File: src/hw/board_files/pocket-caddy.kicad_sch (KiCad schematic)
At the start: 6 parts

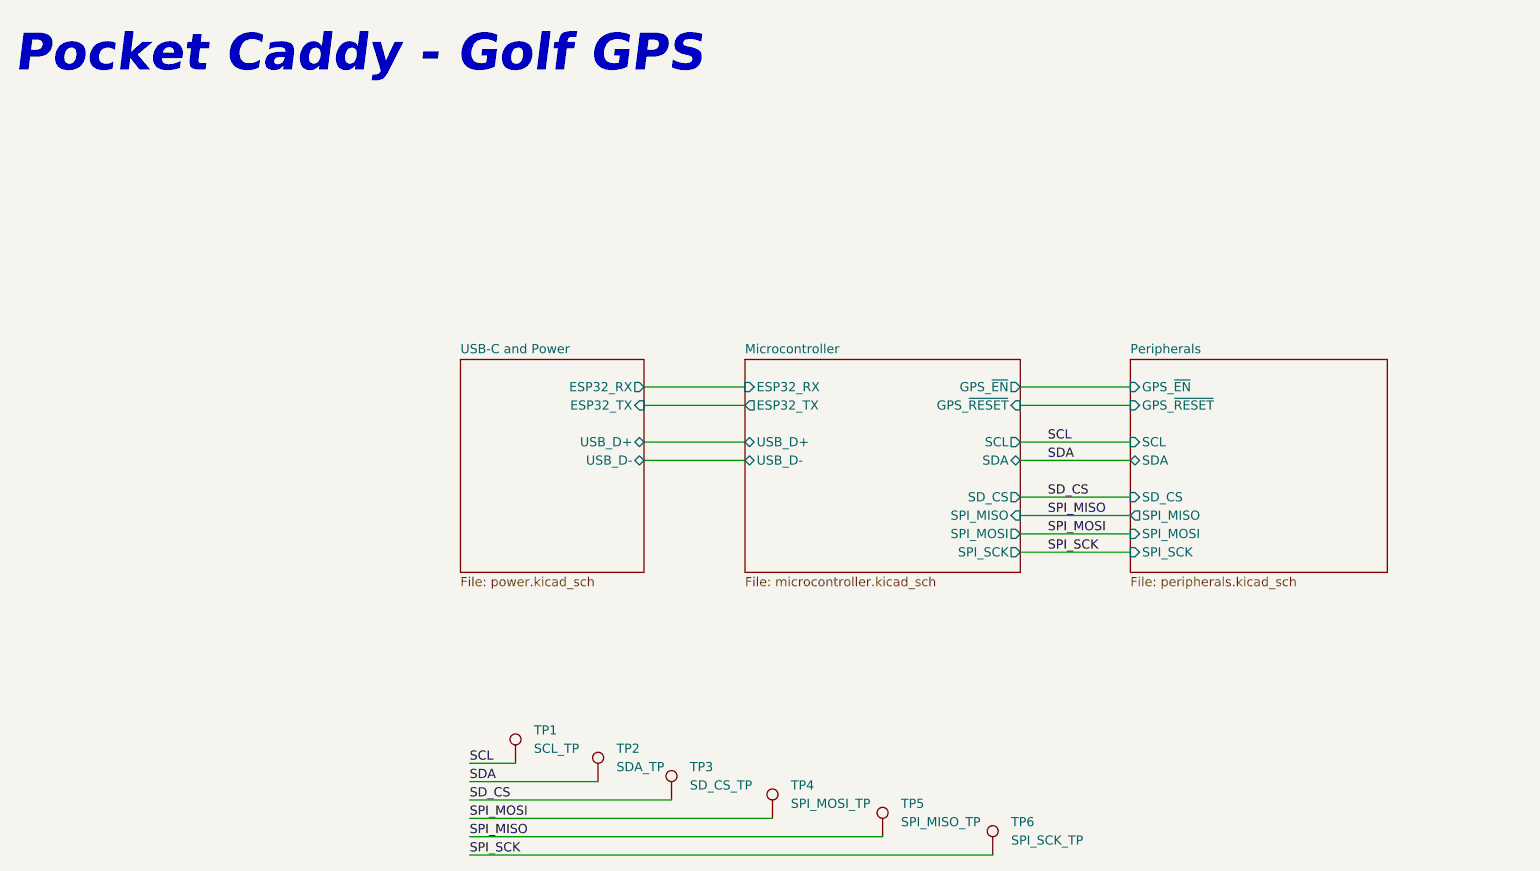
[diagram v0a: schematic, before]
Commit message: Schematic updates
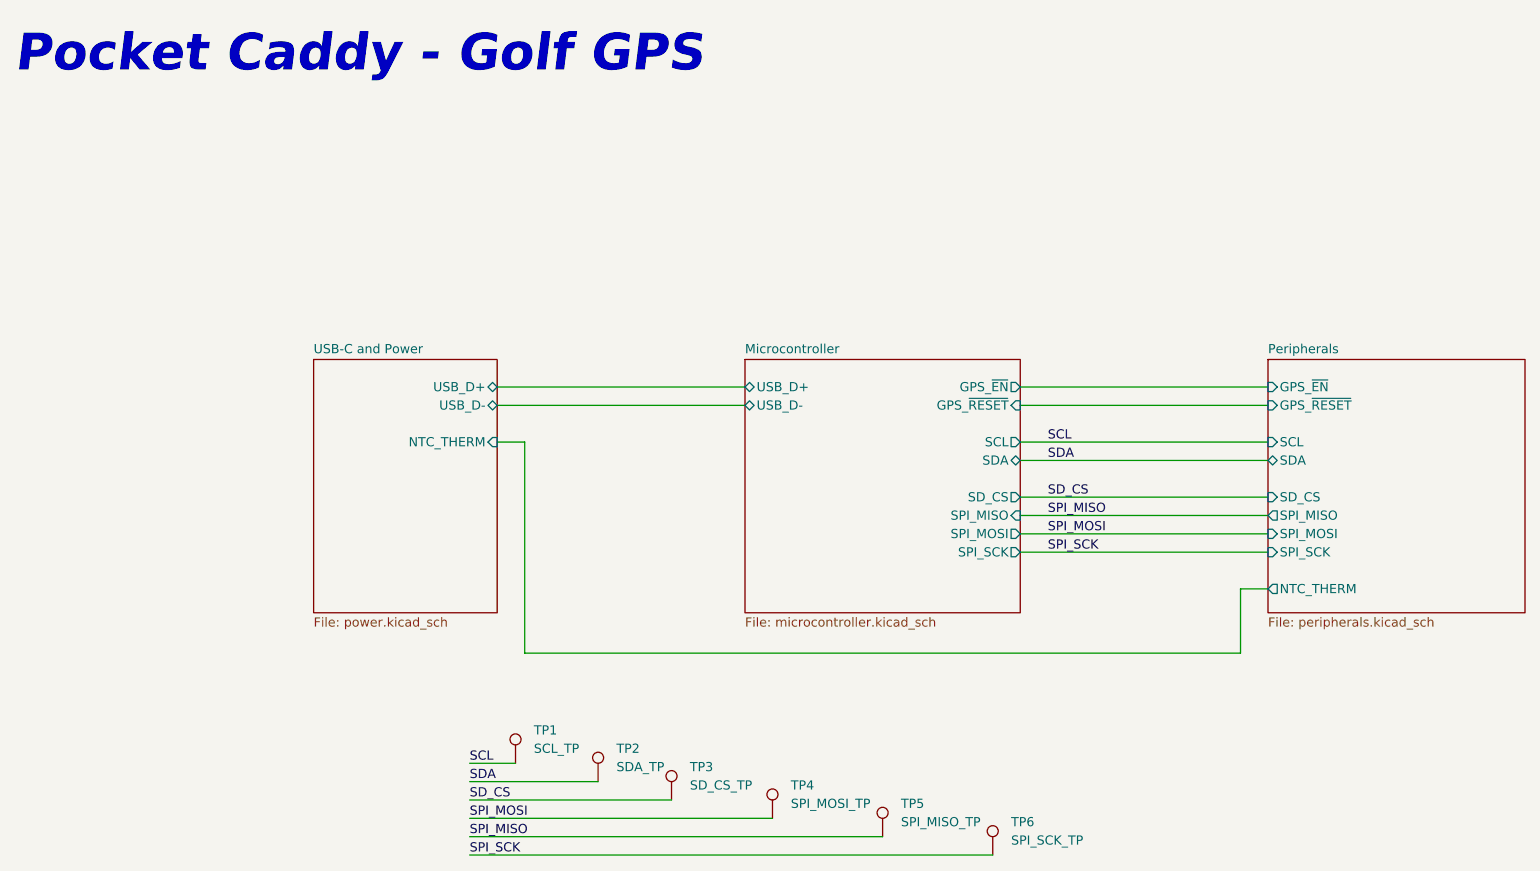
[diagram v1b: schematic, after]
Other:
- sheet Microcontroller ports: added none; removed ESP32_RX, ESP32_TX
- sheet Peripherals ports: added NTC_THERM; removed none
- sheet USB-C and Power ports: added NTC_THERM; removed ESP32_RX, ESP32_TX
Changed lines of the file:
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@@
 	(title_block
 		(title "Pocket Caddy - Golf GPS")
-		(date "2025-10-03")
-		(rev "0")
+		(date "2025-11-15")
+		(rev "0.1")
 		(company "EE 333 - Electronic Systems Design")
 		(comment 1 "B. Kuhn")
@@
 	(wire
 		(pts
-			(xy 153.67 72.39) (xy 168.91 72.39)
+			(xy 153.67 72.39) (xy 187.96 72.39)
 		)
 		(stroke
@@
 	(wire
 		(pts
+			(xy 85.09 72.39) (xy 85.09 101.6)
+		)
+		(stroke
+			(width 0)
+			(type default)
+		)
+	)
+	(wire
+		(pts
 			(xy 77.47 124.46) (xy 119.38 124.46)
 		)
@@
 	(wire
 		(pts
-			(xy 153.67 74.93) (xy 168.91 74.93)
-		)
-		(stroke
-			(width 0)
-			(type default)
-		)
-	)
-	(wire
-		(pts
-			(xy 153.67 64.77) (xy 168.91 64.77)
-		)
-		(stroke
-			(width 0)
-			(type default)
-		)
-	)
-	(wire
-		(pts
-			(xy 153.67 80.01) (xy 168.91 80.01)
+			(xy 153.67 74.93) (xy 187.96 74.93)
+		)
+		(stroke
+			(width 0)
+			(type default)
+		)
+	)
+	(wire
+		(pts
+			(xy 153.67 64.77) (xy 187.96 64.77)
+		)
+		(stroke
+			(width 0)
+			(type default)
+		)
+	)
+	(wire
+		(pts
+			(xy 184.15 101.6) (xy 184.15 92.71)
+		)
+		(stroke
+			(width 0)
+			(type default)
+		)
+	)
+	(wire
+		(pts
+			(xy 85.09 101.6) (xy 184.15 101.6)
+		)
+		(stroke
+			(width 0)
+			(type default)
+		)
+	)
+	(wire
+		(pts
+			(xy 153.67 80.01) (xy 187.96 80.01)
 		)
 		(stroke
@@
 	(wire
 		(pts
-			(xy 153.67 67.31) (xy 168.91 67.31)
-		)
-		(stroke
-			(width 0)
-			(type default)
-		)
-	)
-	(wire
-		(pts
-			(xy 153.67 87.63) (xy 168.91 87.63)
-		)
-		(stroke
-			(width 0)
-			(type default)
-		)
-	)
-	(wire
-		(pts
-			(xy 101.6 67.31) (xy 115.57 67.31)
+			(xy 153.67 67.31) (xy 187.96 67.31)
+		)
+		(stroke
+			(width 0)
+			(type default)
+		)
+	)
+	(wire
+		(pts
+			(xy 153.67 87.63) (xy 187.96 87.63)
+		)
+		(stroke
+			(width 0)
+			(type default)
+		)
+	)
+	(wire
+		(pts
+			(xy 184.15 92.71) (xy 187.96 92.71)
 		)
 		(stroke
@@
 	(wire
 		(pts
-			(xy 153.67 85.09) (xy 168.91 85.09)
+			(xy 153.67 85.09) (xy 187.96 85.09)
 		)
 		(stroke
@@
 	(wire
 		(pts
-			(xy 153.67 82.55) (xy 168.91 82.55)
-		)
-		(stroke
-			(width 0)
-			(type default)
-		)
-	)
-	(wire
-		(pts
-			(xy 101.6 64.77) (xy 115.57 64.77)
+			(xy 81.28 72.39) (xy 85.09 72.39)
+		)
+		(stroke
+			(width 0)
+			(type default)
+		)
+	)
+	(wire
+		(pts
+			(xy 153.67 82.55) (xy 187.96 82.55)
 		)
 		(stroke
@@
 	(wire
 		(pts
-			(xy 101.6 74.93) (xy 115.57 74.93)
-		)
-		(stroke
-			(width 0)
-			(type default)
-		)
-	)
-	(wire
-		(pts
-			(xy 101.6 72.39) (xy 115.57 72.39)
+			(xy 81.28 67.31) (xy 115.57 67.31)
+		)
+		(stroke
+			(width 0)
+			(type default)
+		)
+	)
+	(wire
+		(pts
+			(xy 81.28 64.77) (xy 115.57 64.77)
 		)
 		(stroke
@@
 	(sheet
 		(at 115.57 60.96)
-		(size 38.1 29.464)
+		(size 38.1 35.052)
 		(exclude_from_sim no)
 		(in_bom yes)
@@
 		)
 		(property "Sheetfile" "microcontroller.kicad_sch"
-			(at 115.57 91.0086 0)
+			(at 115.57 96.5966 0)
 			(effects
 				(font
@@
 				)
 				(justify left top)
-			)
-		)
-		(pin "ESP32_RX" input
-			(at 115.57 64.77 180)
-			(effects
-				(font
-					(size 1.27 1.27)
-				)
-				(justify left)
-			)
-		)
-		(pin "ESP32_TX" output
-			(at 115.57 67.31 180)
-			(effects
-				(font
-					(size 1.27 1.27)
-				)
-				(justify left)
 			)
 		)
@@
 		)
 		(pin "USB_D+" bidirectional
-			(at 115.57 72.39 180)
+			(at 115.57 64.77 180)
 			(effects
 				(font
@@
 		)
 		(pin "USB_D-" bidirectional
-			(at 115.57 74.93 180)
+			(at 115.57 67.31 180)
 			(effects
 				(font
@@
 	)
 	(sheet
-		(at 76.2 60.96)
-		(size 25.4 29.464)
+		(at 55.88 60.96)
+		(size 25.4 35.052)
 		(exclude_from_sim no)
 		(in_bom yes)
@@
 		)
 		(property "Sheetname" "USB-C and Power"
-			(at 76.2 60.2484 0)
+			(at 55.88 60.2484 0)
 			(effects
 				(font
@@
 		)
 		(property "Sheetfile" "power.kicad_sch"
-			(at 76.2 91.0086 0)
+			(at 55.88 96.5966 0)
 			(effects
 				(font
@@
 			)
 		)
-		(pin "ESP32_RX" output
-			(at 101.6 64.77 0)
+		(pin "USB_D+" bidirectional
+			(at 81.28 64.77 0)
 			(effects
 				(font
@@
 			)
 		)
-		(pin "ESP32_TX" input
-			(at 101.6 67.31 0)
+		(pin "USB_D-" bidirectional
+			(at 81.28 67.31 0)
 			(effects
 				(font
@@
 			)
 		)
-		(pin "USB_D+" bidirectional
-			(at 101.6 72.39 0)
-			(effects
-				(font
-					(size 1.27 1.27)
-				)
-				(justify right)
-			)
-		)
-		(pin "USB_D-" bidirectional
-			(at 101.6 74.93 0)
+		(pin "NTC_THERM" input
+			(at 81.28 72.39 0)
 			(effects
 				(font
@@
 	)
 	(sheet
-		(at 168.91 60.96)
-		(size 35.56 29.464)
+		(at 187.96 60.96)
+		(size 35.56 35.052)
 		(exclude_from_sim no)
 		(in_bom yes)
@@
 		)
 		(property "Sheetname" "Peripherals"
-			(at 168.91 60.2484 0)
+			(at 187.96 60.2484 0)
 			(effects
 				(font
@@
 		)
 		(property "Sheetfile" "peripherals.kicad_sch"
-			(at 168.91 91.0086 0)
+			(at 187.96 96.5966 0)
 			(effects
 				(font
@@
 		)
 		(pin "GPS_~{EN}" input
-			(at 168.91 64.77 180)
+			(at 187.96 64.77 180)
 			(effects
 				(font
@@
 		)
 		(pin "GPS_~{RESET}" input
-			(at 168.91 67.31 180)
+			(at 187.96 67.31 180)
 			(effects
 				(font
@@
 		)
 		(pin "SCL" input
-			(at 168.91 72.39 180)
+			(at 187.96 72.39 180)
 			(effects
 				(font
@@
 		)
 		(pin "SDA" bidirectional
-			(at 168.91 74.93 180)
+			(at 187.96 74.93 180)
 			(effects
 				(font
@@
 		)
 		(pin "SD_CS" input
-			(at 168.91 80.01 180)
+			(at 187.96 80.01 180)
 			(effects
 				(font
@@
 		)
 		(pin "SPI_MISO" output
-			(at 168.91 82.55 180)
+			(at 187.96 82.55 180)
 			(effects
 				(font
@@
 		)
 		(pin "SPI_MOSI" input
-			(at 168.91 85.09 180)
+			(at 187.96 85.09 180)
 			(effects
 				(font
@@
 		)
 		(pin "SPI_SCK" input
-			(at 168.91 87.63 180)
-			(effects
-				(font
+			(at 187.96 87.63 180)
+			(effects
+				(font
+					(size 1.27 1.27)
+				)
+				(justify left)
+			)
+		)
+		(pin "NTC_THERM" output
+			(at 187.96 92.71 180)
+			(effects
+				(font

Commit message: Layout progress
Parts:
- TP1, TP2, TP3, TP4, TP5, TP6: footprint TestPoint:TestPoint_Pad_D1.5mm -> TestPoint:TestPoint_Pad_D1.0mm
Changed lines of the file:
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@@
 			)
 		)
-		(property "Footprint" "TestPoint:TestPoint_Pad_D1.5mm"
+		(property "Footprint" "TestPoint:TestPoint_Pad_D1.0mm"
 			(at 139.7 127 0)
 			(effects
@@
 			)
 		)
-		(property "Footprint" "TestPoint:TestPoint_Pad_D1.5mm"
+		(property "Footprint" "TestPoint:TestPoint_Pad_D1.0mm"
 			(at 154.94 129.54 0)
 			(effects
@@
 			)
 		)
-		(property "Footprint" "TestPoint:TestPoint_Pad_D1.5mm"
+		(property "Footprint" "TestPoint:TestPoint_Pad_D1.0mm"
 			(at 124.46 124.46 0)
 			(effects
@@
 			)
 		)
-		(property "Footprint" "TestPoint:TestPoint_Pad_D1.5mm"
+		(property "Footprint" "TestPoint:TestPoint_Pad_D1.0mm"
 			(at 100.33 119.38 0)
 			(effects
@@
 			)
 		)
-		(property "Footprint" "TestPoint:TestPoint_Pad_D1.5mm"
+		(property "Footprint" "TestPoint:TestPoint_Pad_D1.0mm"
 			(at 110.49 121.92 0)
 			(effects
@@
 			)
 		)
-		(property "Footprint" "TestPoint:TestPoint_Pad_D1.5mm"
+		(property "Footprint" "TestPoint:TestPoint_Pad_D1.0mm"
 			(at 88.9 116.84 0)
 			(effects

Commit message: Layout progress
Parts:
- removed TP3: SD_CS_TP, TestPoint:TestPoint_Pad_D1.0mm, symbol Connector:TestPoint
- removed TP4: SPI_MOSI_TP, TestPoint:TestPoint_Pad_D1.0mm, symbol Connector:TestPoint
- removed TP5: SPI_MISO_TP, TestPoint:TestPoint_Pad_D1.0mm, symbol Connector:TestPoint
- removed TP6: SPI_SCK_TP, TestPoint:TestPoint_Pad_D1.0mm, symbol Connector:TestPoint
